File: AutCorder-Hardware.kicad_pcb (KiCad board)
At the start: 4 copper layers, 23.7 x 33 mm, 64 parts, among them J1 Battery, J2 OV2640, J3 EXT LED, J4 Shutter, J5 Util, J6 Feedback, J7 Micro SD, J8 PWR_ALT, P1 USB_C_Plug_USB2.0, Q1 DMP2045U, Q2 DMP2045U, Q3 DMN2040U, SW1 FW, SW2 RESET, U1 ESP32-S3-WROOM-1, U2 MCP73831-2-OT, U3 XC6220B331MR, U4 XC6206P282MR, U5 XC6206P122MR, U6 IMP34DT05TR

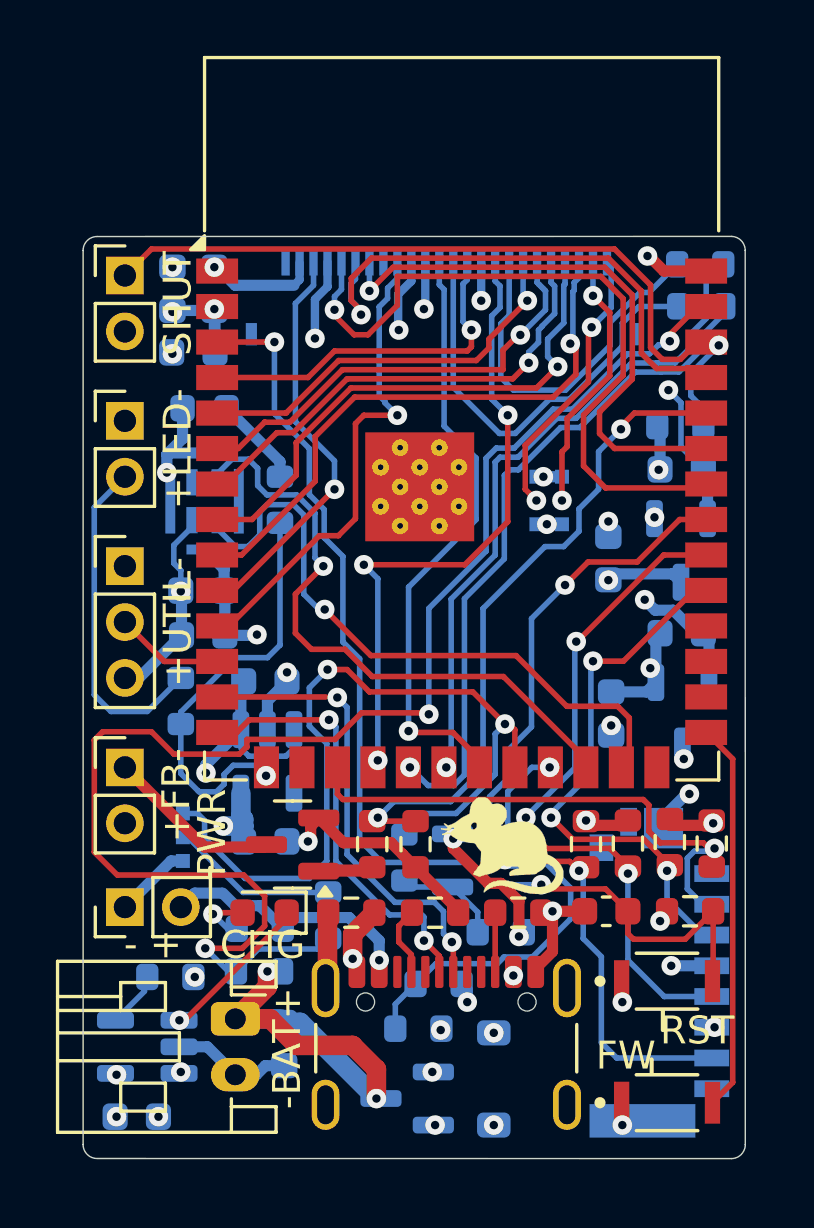
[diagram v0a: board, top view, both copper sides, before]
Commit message: Switched R5, Fixed USB data, Removed J3, Removed R10, Reoriented J1, Rearranged components.
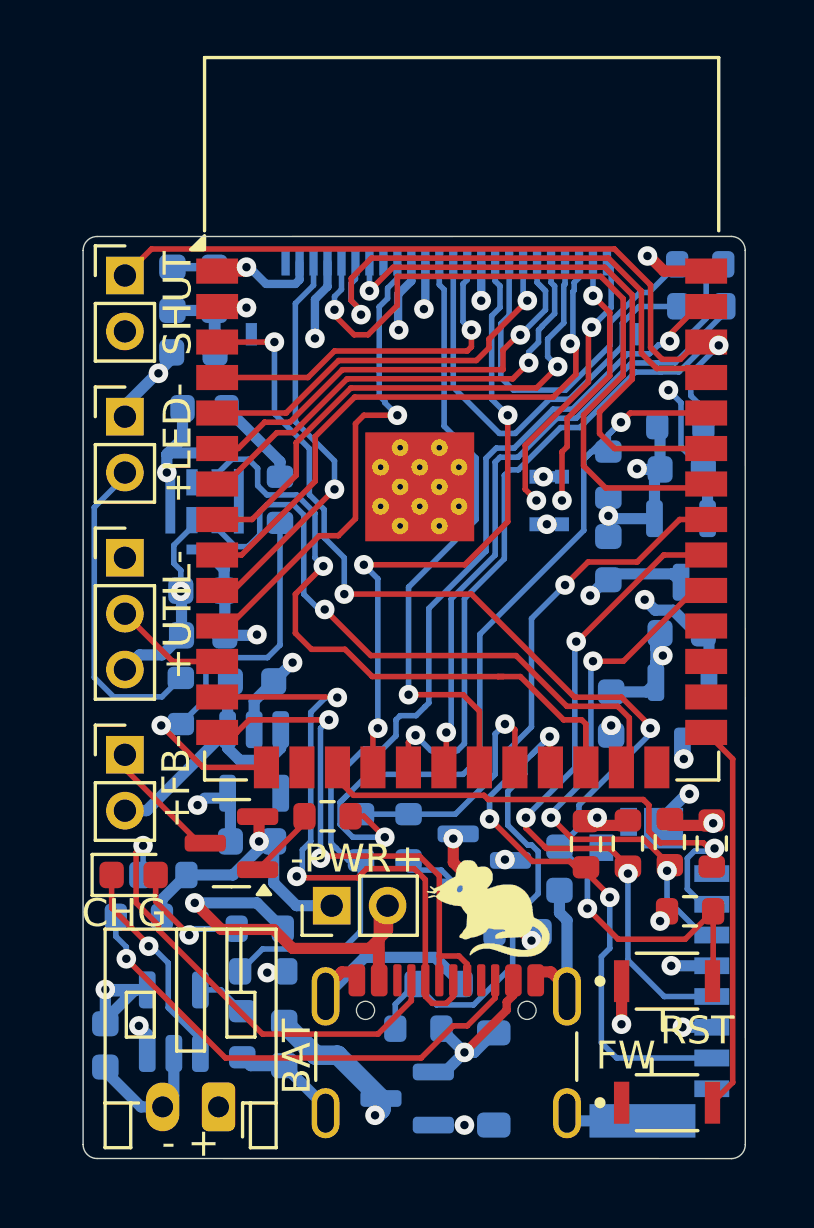
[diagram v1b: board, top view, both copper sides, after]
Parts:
- removed JP3: BatRegLevelSelect, 10067099-200LF:SolderJumper-3_P0.75mm_Open_Pad0.5x1mm
- removed R10: 0, Resistor_SMD:R_0603_1608Metric
- C10, R11, R12, R15: moved to B.Cu
- P1: value USB_C_Plug_USB2.0 -> USB_C_Receptacle_USB2.0_16P
- R5: value 100k -> 50k
- moved R15 14.9 mm to (55.8, 52.0)
- moved R12 13.6 mm to (39.0, 67.8)
- moved R11 9.82 mm to (39.9, 66.3)
- moved J8 7.40 mm to (45.9, 67.5)
- moved D1 4.88 mm to (38.8, 66.3), turned to 0 degrees
- moved R1 3.29 mm to (42.7, 72.0), turned to -90 degrees
- moved J1 3.21 mm to (41.9, 74.7), turned to 180 degrees
- moved R22 3.04 mm to (47.0, 65.0)
- moved C1 2.79 mm to (37.8, 72.5), turned to -90 degrees
- moved G*** 2.30 mm to (51.5, 67.2)
- moved C10 2.27 mm to (54.0, 66.1), turned to -90 degrees
- moved Q3 2.19 mm to (42.3, 65.2)
- moved R14 1.89 mm to (45.8, 64.2), turned to 180 degrees
- moved U2 1.31 mm to (40.2, 71.6), turned to 90 degrees
- moved R13 0.74 mm to (48.6, 65.0)
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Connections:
- P1 pad A8: (no net) -> unconnected-(P1-SBU1-PadA8)
- P1 pad B6: (no net) -> /USB_D+
- P1 pad B7: (no net) -> /USB_D-
- P1 pad B8: (no net) -> unconnected-(P1-SBU2-PadB8)
- P1 pad S1: Net-(P1-SHIELD) -> -BATT
- R22 pad 1: Net-(JP3-C) -> /PERIPH_PWR
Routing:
- net -BATT: track 49.8 -> 97.5 mm, vias 23 -> 15
- net Net-(P1-SHIELD): track 20.7 -> 0.00 mm
- net /PERIPH_PWR: track 29.4 -> 9.34 mm, vias 2 -> 1
- net /BAT_LEVEL_I: track 52.5 -> 35.2 mm, vias 3 -> 1
- net Net-(P1-CC2): track 2.12 -> 18.0 mm, vias 0 -> 1
- net Net-(P1-CC1): track 2.50 -> 16.5 mm, vias 0 -> 1
- net VBUS: track 26.8 -> 40.6 mm, vias 7 -> 3
- net +3V3: track 57.0 -> 64.7 mm, vias 6 -> 5
- net /FEEDBACK_O: track 23.7 -> 29.8 mm
- net /USB_D-: track 16.3 -> 22.3 mm
- net Net-(JP3-C): track 6.02 -> 0.00 mm
- net +BATT: track 30.3 -> 25.1 mm
- net Net-(D1-A): track 2.08 -> 6.43 mm
- net /USB_D+: track 15.5 -> 19.6 mm
- net Net-(U1-EN): track 38.6 -> 41.3 mm, vias 2 -> 4
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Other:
- board text added: "-PWR+"
- board text added: "2025"
- board text added: "AutCorder V2.1"
- board text added: "BAT"
- board text removed: "-BAT+"
- board text removed: "2024"
- board text removed: "AutCorder V2.0"
- board text removed: "PWR"

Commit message: Switched to slimmer FPC connector. Rerouted.
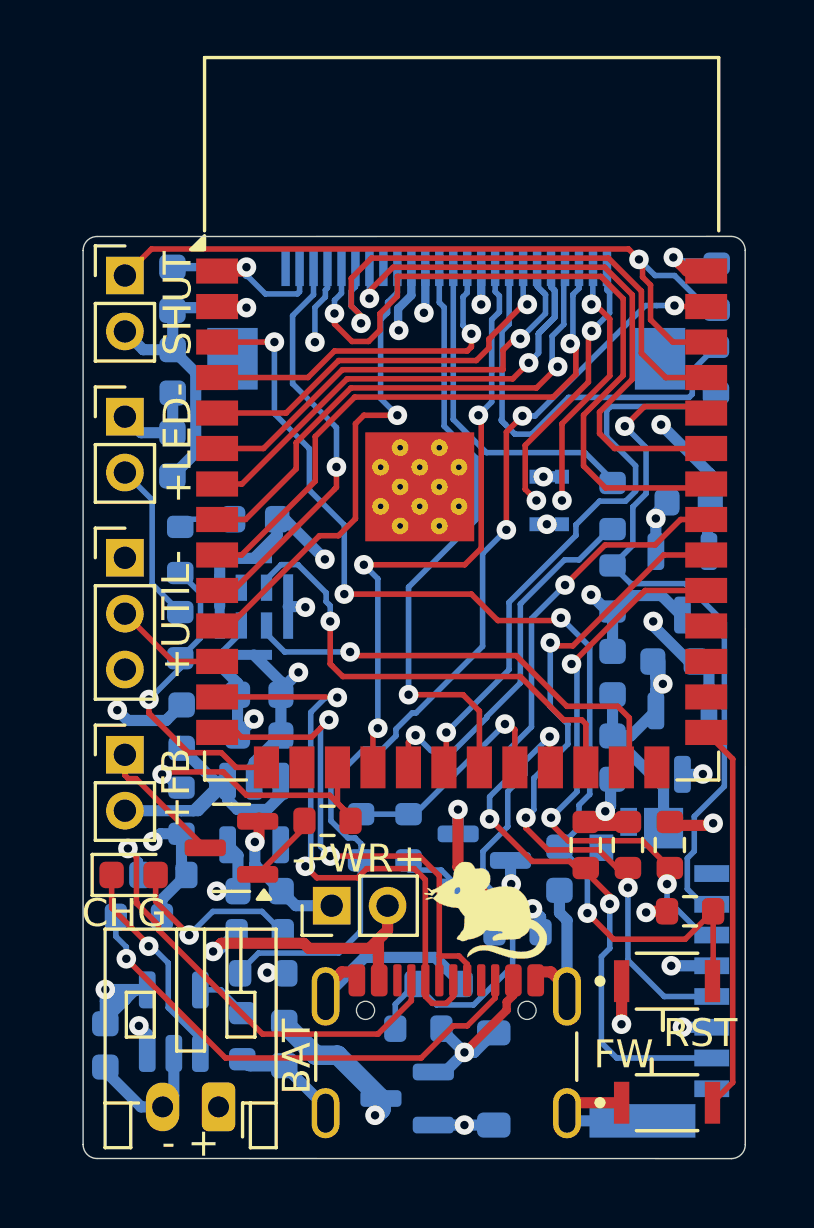
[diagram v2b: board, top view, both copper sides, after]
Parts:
- J2: footprint CF35242D0RD-NH:CVILUX_CF35242D0RD-NH -> FFC2B35-24-G:CONN_FFC2B35-24-x_GCT
- R6: moved to B.Cu
- moved R15 19.4 mm to (40.5, 64.0)
- moved R6 9.79 mm to (56.0, 56.1), turned to 90 degrees
- moved R3 7.82 mm to (56.0, 53.1), turned to 90 degrees
- moved C13 5.57 mm to (43.3, 61.4)
- moved R17 5.15 mm to (59.7, 45.3), turned to 90 degrees
- moved D3 4.36 mm to (43.2, 53.6), turned to 180 degrees
- moved U6 4.16 mm to (43.1, 56.7)
- moved C8 4.12 mm to (56.0, 59.1), turned to -90 degrees
- moved R19 4.00 mm to (40.5, 54.7)
- moved R2 3.82 mm to (59.6, 48.3), turned to 90 degrees
- moved C11 3.73 mm to (40.2, 51.3), turned to 90 degrees
- moved C9 3.31 mm to (40.2, 48.3), turned to -90 degrees
- moved C3 2.99 mm to (40.5, 61.0), turned to 90 degrees
- moved C14 2.92 mm to (43.3, 59.9)
- moved R23 2.36 mm to (40.5, 57.8)
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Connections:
- J2 pad 1: unconnected-(J2-Pad1) -> Net-(JP2-C)
- J2 pad 10: +1V2 -> -BATT
- J2 pad 11: +2V8 -> /CAM_Y8
- J2 pad 12: /CAM_Y9 -> Net-(J2-Pad12)
- J2 pad 13: Net-(J2-Pad13) -> /CAM_Y9
- J2 pad 14: /CAM_Y8 -> +2V8
- J2 pad 15: -BATT -> +1V2
- J2 pad 16: /CAM_Y7 -> /CAM_HREF
- J2 pad 17: Net-(J2-Pad17) -> /CAM_PWDN
- J2 pad 18: /CAM_Y6 -> /CAM_VSYNC
- J2 pad 19: /CAM_Y2 -> /CAM_RESET
- J2 pad 2: -BATT -> Net-(JP1-C)
- J2 pad 20: /CAM_Y5 -> /CAM_SIO_C
- J2 pad 21: /CAM_Y3 -> +2V8
- J2 pad 22: /CAM_Y4 -> /CAM_SIO_D
- J2 pad 23: Net-(JP1-C) -> -BATT
- J2 pad 24: Net-(JP2-C) -> unconnected-(J2-Pad24)
- J2 pad 3: /CAM_SIO_D -> /CAM_Y4
- J2 pad 4: +2V8 -> /CAM_Y3
- J2 pad 5: /CAM_SIO_C -> /CAM_Y5
- J2 pad 6: /CAM_RESET -> /CAM_Y2
- J2 pad 7: /CAM_VSYNC -> /CAM_Y6
- J2 pad 8: /CAM_PWDN -> Net-(J2-Pad8)
- J2 pad 9: /CAM_HREF -> /CAM_Y7
- R2 pad 2: Net-(J2-Pad17) -> Net-(J2-Pad8)
- R3 pad 2: Net-(J2-Pad13) -> Net-(J2-Pad12)
- U1 pad 17: /SPI_CS -> /FEEDBACK_O
- U1 pad 36: /FEEDBACK_O -> /SPI_CS
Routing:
- net /FEEDBACK_O: track 29.8 -> 10.2 mm, vias 2 -> 1
- net +3V3SW: track 64.1 -> 81.5 mm, vias 8 -> 7
- net Net-(J2-Pad13): track 15.6 -> 0.00 mm
- net Net-(J2-Pad8): track 0.00 -> 15.5 mm
- net Net-(J2-Pad17): track 13.1 -> 0.00 mm
- net Net-(J2-Pad12): track 0.00 -> 12.2 mm
- net /CAM_XVCLK: track 24.3 -> 13.5 mm
- net -BATT: track 97.5 -> 106.9 mm, vias 15 -> 14
- net /MIC_DATA: track 22.7 -> 15.7 mm
- net /MIC_CLK: track 23.2 -> 17.0 mm
- net Net-(J3-Pin_2): track 11.3 -> 5.82 mm
- net /SPI_CS: track 19.0 -> 24.5 mm
- net VBUS: track 40.6 -> 35.3 mm
- net /CAM_Y5: track 16.7 -> 22.0 mm
- net /LED_O: track 14.8 -> 11.1 mm
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- added copper zone on In1.Cu, net +1V2
- added copper zone on In1.Cu, net +2V8
- added copper zone on In1.Cu, net +3V3
- added copper zone on In1.Cu, net +3V3SW
- added copper zone on In1.Cu, net +BATT
- added copper zone on In1.Cu, net VBATBUS
- added copper zone on In1.Cu, net VBUS
